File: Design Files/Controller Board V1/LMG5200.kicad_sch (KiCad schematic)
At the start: 4 parts, among them Q1 LMG5200

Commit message: yay(meeting 2/16/2025)
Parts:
- removed R1: R, symbol Device:R
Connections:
- net ADC1 renamed ADC_Pos
- net ADC3 renamed ADC_Neg
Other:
- moved on the sheet: L2
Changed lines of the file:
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@@
 	(paper "A4")
-	(junction
-		(at 139.7 81.28)
-		(diameter 0)
-		(color 0 0 0 0)
-	)
-	(junction
-		(at 139.7 71.12)
-		(diameter 0)
-		(color 0 0 0 0)
-	)
 	(junction
 		(at 139.7 66.04)
@@
 		(color 0 0 0 0)
 	)
-	(junction
-		(at 139.7 62.23)
-		(diameter 0)
-		(color 0 0 0 0)
-	)
 	(wire
 		(pts
@@
 	(wire
 		(pts
-			(xy 139.7 83.82) (xy 139.7 81.28)
+			(xy 143.51 83.82) (xy 143.51 81.28)
 		)
 		(stroke
@@
 	(wire
 		(pts
-			(xy 139.7 52.07) (xy 139.7 62.23)
-		)
-		(stroke
-			(width 0)
-			(type default)
-		)
-	)
-	(wire
-		(pts
 			(xy 143.51 125.73) (xy 143.51 134.62)
 		)
@@
 	(wire
 		(pts
-			(xy 139.7 81.28) (xy 139.7 78.74)
-		)
-		(stroke
-			(width 0)
-			(type default)
-		)
-	)
-	(wire
-		(pts
 			(xy 139.7 71.12) (xy 139.7 66.04)
 		)
@@
 	(wire
 		(pts
-			(xy 139.7 81.28) (xy 153.67 81.28)
+			(xy 143.51 81.28) (xy 153.67 81.28)
 		)
 		(stroke
@@
 		)
 	)
-	(hierarchical_label "ADC3"
+	(hierarchical_label "ADC_Neg"
 		(shape input)
 		(at 153.67 81.28 0)
@@
 		)
 	)
-	(hierarchical_label "ADC1"
-		(shape input)
-		(at 139.7 52.07 90)
-		(effects
-			(font
-				(size 1.27 1.27)
-			)
-			(justify left)
-		)
-	)
 	(hierarchical_label "bottom_out"
 		(shape input)
@@
 		)
 	)
-	(hierarchical_label "ADC2"
+	(hierarchical_label "ADC_Pos"
 		(shape input)
 		(at 153.67 71.12 0)
@@
 	(symbol
 		(lib_id "Device:L")
-		(at 139.7 87.63 0)
+		(at 143.51 87.63 0)
 		(unit 1)
 		(exclude_from_sim no)
@@
 		(fields_autoplaced yes)
 		(property "Reference" "L2"
-			(at 140.97 86.3599 0)
+			(at 144.78 86.3599 0)
 			(effects
 				(font
@@
 		)
 		(property "Value" "L"
-			(at 140.97 88.8999 0)
+			(at 144.78 88.8999 0)
 			(effects
 				(font
@@
 		)
 		(property "Footprint" ""
-			(at 139.7 87.63 0)
+			(at 143.51 87.63 0)
 			(effects
 				(font
@@
 		)
 		(property "Datasheet" "~"
-			(at 139.7 87.63 0)
+			(at 143.51 87.63 0)
 			(effects
 				(font
@@
 		)
 		(property "Description" "Inductor"
-			(at 139.7 87.63 0)
+			(at 143.51 87.63 0)
 			(effects
 				(font
@@
 					(unit 1)
 				)
-			)
-		)
-	)
-	(symbol
-		(lib_id "Device:R")
-		(at 139.7 74.93 0)
-		(unit 1)
-		(exclude_from_sim no)
-		(in_bom yes)
-		(on_board yes)
-		(dnp no)
-		(fields_autoplaced yes)
-		(property "Reference" "R1"
-			(at 142.24 73.6599 0)
-			(effects
-				(font
-					(size 1.27 1.27)
-				)
-				(justify left)
-			)
-		)
-		(property "Value" "R"
-			(at 142.24 76.1999 0)
-			(effects
-				(font
-					(size 1.27 1.27)
-				)
-				(justify left)
-			)
-		)
-		(property "Footprint" ""
-			(at 137.922 74.93 90)
-			(effects
-				(font
-					(size 1.27 1.27)
-				)
-				(hide yes)
-			)
-		)
-		(property "Datasheet" "~"
-			(at 139.7 74.93 0)
-			(effects
-				(font
-					(size 1.27 1.27)
-				)
-				(hide yes)
-			)
-		)
-		(property "Description" "Resistor"
-			(at 139.7 74.93 0)
-			(effects
-				(font
-					(size 1.27 1.27)
-				)
-				(hide yes)
-			)
-		)
-		(pin "1"
-		)
-		(pin "2"
-		)
-		(instances
-			(project "Control Board V1"
-				(path "/e0c606b8-cbb9-4aff-b96c-73876da6ca74/a6c70f8b-d576-48c3-bfc7-6e0bdb401246"
-					(reference "R1")
-					(unit 1)
-				)

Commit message: Major Schematic Progress
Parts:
- added C2, C3: 0.1u, symbol Device:C
- added R1: 39k, Resistor_SMD:R_0603_1608Metric, symbol Device:R
- added R13, R14: 2k, Resistor_SMD:R_0603_1608Metric, symbol Device:R
- added R15: 11k, Resistor_SMD:R_0603_1608Metric, symbol Device:R
- C1: value C -> 10u
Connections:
- net ADC_Neg is gone; now on an unnamed net: L2.1
- net ADC_Pos is gone; now on net cap_volt: C1.2
- net 5V: now also C2.1
- net GND: now also Q1.9, R15.2
- net PWM_bottom: now also R13.1
- net PWM_top: now also R14.1
- net cap_volt: now reaches L2.2
- net cap_volt: now also R1.1
- net high_side_FET: now reaches Q1.1
- net at Q1.2 (HB): now also C3.1
- net at Q1.3 (HS): now also C3.2
- net sig-gnd renamed A_GND
- net A_GND: now also C2.2, R13.2, R14.2
- new net cap_volt_pico_adc: R1.2, R15.1
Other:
- moved on the sheet: C1, L2, Q1

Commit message: here we go agane
Updating footprints and tackling general layout
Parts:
- C2, C3: footprint (none) -> Capacitor_SMD:C_0603_1608Metric
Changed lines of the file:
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@@
 			)
 		)
-		(property "Footprint" ""
+		(property "Footprint" "Capacitor_SMD:C_0603_1608Metric"
 			(at 108.9152 96.52 0)
 			(effects
@@
 			)
 		)
-		(property "Footprint" ""
+		(property "Footprint" "Capacitor_SMD:C_0603_1608Metric"
 			(at 113.03 84.7852 0)
 			(effects

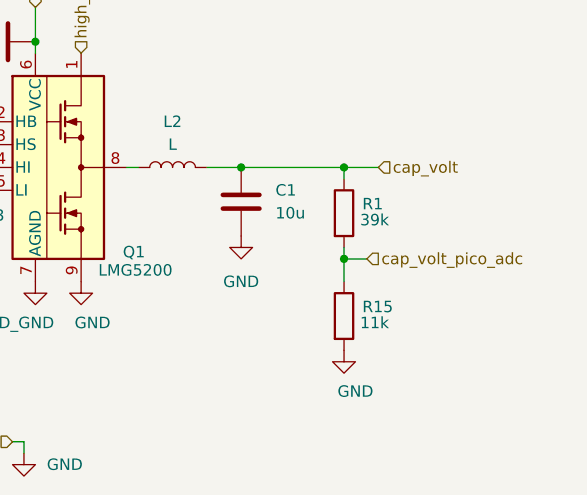
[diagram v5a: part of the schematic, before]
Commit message: current sensor done
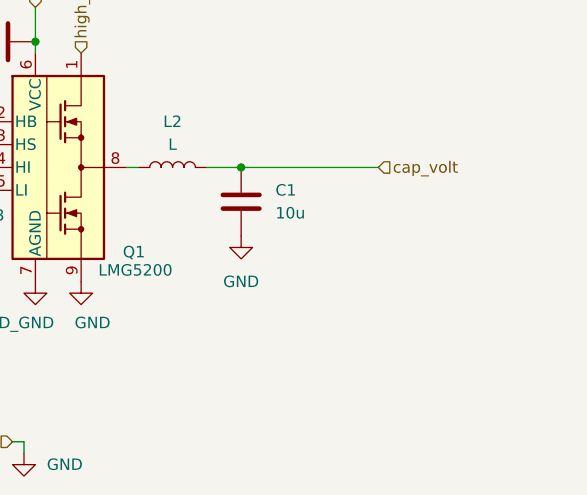
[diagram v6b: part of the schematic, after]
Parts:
- removed R1: 39k, Resistor_SMD:R_0603_1608Metric, symbol Device:R
- removed R15: 11k, Resistor_SMD:R_0603_1608Metric, symbol Device:R

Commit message: Added Cap footprint, added LED, added Resistors
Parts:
- C1: footprint (none) -> Capacitor_SMD:C_0603_1608Metric
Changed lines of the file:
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@@
 		(shape input)
 		(at 158.75 97.79 0)
+		(fields_autoplaced yes)
 		(effects
 			(font
@@
 		(shape input)
 		(at 95.25 128.27 180)
+		(fields_autoplaced yes)
 		(effects
 			(font
@@
 		(shape input)
 		(at 120.65 80.01 90)
+		(fields_autoplaced yes)
 		(effects
 			(font
@@
 		(shape input)
 		(at 118.11 128.27 180)
+		(fields_autoplaced yes)
 		(effects
 			(font
@@
 		(shape input)
 		(at 110.49 100.33 180)
+		(fields_autoplaced yes)
 		(effects
 			(font
@@
 		(shape input)
 		(at 88.9 97.79 180)
+		(fields_autoplaced yes)
 		(effects
 			(font
@@
 		(shape input)
 		(at 125.73 85.09 90)
+		(fields_autoplaced yes)
 		(effects
 			(font
@@
 			)
 		)
-		(property "Footprint" ""
+		(property "Footprint" "Capacitor_SMD:C_0603_1608Metric"
 			(at 142.5448 97.79 0)
 			(effects

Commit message: half finished with brooks changes
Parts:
- added C12: 10u, Capacitor_SMD:C_0603_1608Metric, symbol Device:C
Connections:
- net GND: now also C12.1; no longer C1.1, Q1.9
- net A_GND renamed D_GND
- net D_GND: no longer Q1.7 (AGND)
- new net P_GND: C1.1, Q1.7 (AGND), Q1.9
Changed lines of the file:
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@@
-	(wire
-		(pts
-			(xy 97.79 129.54) (xy 97.79 128.27)
-		)
-		(stroke
-			(width 0)
-			(type default)
-		)
-	)
 	(wire
 		(pts
@@
 	(wire
 		(pts
-			(xy 119.38 128.27) (xy 118.11 128.27)
-		)
-		(stroke
-			(width 0)
-			(type default)
-		)
-	)
-	(wire
-		(pts
 			(xy 130.81 97.79) (xy 132.08 97.79)
 		)
@@
 	(wire
 		(pts
-			(xy 97.79 128.27) (xy 95.25 128.27)
-		)
-		(stroke
-			(width 0)
-			(type default)
-		)
-	)
-	(wire
-		(pts
-			(xy 119.38 128.27) (xy 119.38 129.54)
+			(xy 125.73 86.36) (xy 132.08 86.36)
 		)
 		(stroke
@@
 		)
 	)
-	(hierarchical_label "D_GND"
-		(shape input)
-		(at 95.25 128.27 180)
-		(fields_autoplaced yes)
-		(effects
-			(font
-				(size 1.27 1.27)
-			)
-			(justify right)
-		)
-	)
 	(hierarchical_label "5V"
 		(shape input)
@@
 		)
 	)
-	(hierarchical_label "P_GND"
-		(shape input)
-		(at 118.11 128.27 180)
-		(fields_autoplaced yes)
-		(effects
-			(font
-				(size 1.27 1.27)
-			)
-			(justify right)
-		)
-	)
 	(hierarchical_label "PWM_bottom"
 		(shape input)
@@
 			)
 		)
-		(property "Value" "GND"
+		(property "Value" "P_GND"
 			(at 127 115.062 0)
 			(effects
@@
 	(symbol
 		(lib_id "Device:C")
+		(at 135.89 86.36 270)
+		(unit 1)
+		(exclude_from_sim no)
+		(in_bom yes)
+		(on_board yes)
+		(dnp no)
+		(fields_autoplaced yes)
+		(property "Reference" "C12"
+			(at 134.6199 82.55 0)
+			(effects
+				(font
+					(size 1.27 1.27)
+				)
+				(justify right)
+			)
+		)
+		(property "Value" "10u"
+			(at 137.1599 82.55 0)
+			(effects
+				(font
+					(size 1.27 1.27)
+				)
+				(justify right)
+			)
+		)
+		(property "Footprint" "Capacitor_SMD:C_0603_1608Metric"
+			(at 132.08 87.3252 0)
+			(effects
+				(font
+					(size 1.27 1.27)
+				)
+				(hide yes)
+			)
+		)
+		(property "Datasheet" "~"
+			(at 135.89 86.36 0)
+			(effects
+				(font
+					(size 1.27 1.27)
+				)
+				(hide yes)
+			)
+		)
+		(property "Description" "Unpolarized capacitor"
+			(at 135.89 86.36 0)
+			(effects
+				(font
+					(size 1.27 1.27)
+				)
+				(hide yes)
+			)
+		)
+		(pin "1"
+		)
+		(pin "2"
+		)
+		(instances
+			(project "Control Board V1"
+				(path "/e0c606b8-cbb9-4aff-b96c-73876da6ca74/a6c70f8b-d576-48c3-bfc7-6e0bdb401246"
+					(reference "C12")
+					(unit 1)
+				)
+			)
+		)
+	)
+	(symbol
+		(lib_id "Device:C")
 		(at 107.95 92.71 0)
 		(unit 1)
@@
 				(path "/e0c606b8-cbb9-4aff-b96c-73876da6ca74/a6c70f8b-d576-48c3-bfc7-6e0bdb401246"
 					(reference "C3")
-					(unit 1)
-				)
-			)
-		)
-	)
-	(symbol
-		(lib_id "power:GND")
-		(at 97.79 129.54 0)
-		(unit 1)
-		(exclude_from_sim no)
-		(in_bom yes)
-		(on_board yes)
-		(dnp no)
-		(property "Reference" "#PWR014"
-			(at 97.79 135.89 0)
-			(effects
-				(font
-					(size 1.27 1.27)
-				)
-				(hide yes)
-			)
-		)
-		(property "Value" "A_GND"
-			(at 103.124 130.81 0)
-			(effects
-				(font
-					(size 1.27 1.27)
-				)
-			)
-		)
-		(property "Footprint" ""
-			(at 97.79 129.54 0)
-			(effects
-				(font
-					(size 1.27 1.27)
-				)
-				(hide yes)
-			)
-		)
-		(property "Datasheet" ""
-			(at 97.79 129.54 0)
-			(effects
-				(font
-					(size 1.27 1.27)
-				)
-				(hide yes)
-			)
-		)
-		(property "Description" "Power symbol creates a global label with name \"GND\" , ground"
-			(at 97.79 129.54 0)
-			(effects
-				(font
-					(size 1.27 1.27)
-				)
-				(hide yes)
-			)
-		)
-		(pin "1"
-		)
-		(instances
-			(project "Control Board V1"
-				(path "/e0c606b8-cbb9-4aff-b96c-73876da6ca74/a6c70f8b-d576-48c3-bfc7-6e0bdb401246"
-					(reference "#PWR014")
-					(unit 1)
-				)
-			)
-		)
-	)
-	(symbol
-		(lib_id "power:GND")
-		(at 119.38 129.54 0)
-		(unit 1)
-		(exclude_from_sim no)
-		(in_bom yes)
-		(on_board yes)
-		(dnp no)
-		(fields_autoplaced yes)
-		(property "Reference" "#PWR01"
-			(at 119.38 135.89 0)
-			(effects
-				(font
-					(size 1.27 1.27)
-				)
-				(hide yes)
-			)
-		)
-		(property "Value" "GND"
-			(at 121.92 130.8099 0)
-			(effects
-				(font
-					(size 1.27 1.27)
-				)
-				(justify left)
-			)
-		)
-		(property "Footprint" ""
-			(at 119.38 129.54 0)
-			(effects
-				(font
-					(size 1.27 1.27)
-				)
-				(hide yes)
-			)
-		)
-		(property "Datasheet" ""
-			(at 119.38 129.54 0)
-			(effects
-				(font
-					(size 1.27 1.27)
-				)
-				(hide yes)
-			)
-		)
-		(property "Description" "Power symbol creates a global label with name \"GND\" , ground"
-			(at 119.38 129.54 0)
-			(effects
-				(font
-					(size 1.27 1.27)
-				)
-				(hide yes)
-			)
-		)
-		(pin "1"
-		)
-		(instances
-			(project "Control Board V1"
-				(path "/e0c606b8-cbb9-4aff-b96c-73876da6ca74/a6c70f8b-d576-48c3-bfc7-6e0bdb401246"
-					(reference "#PWR01")
 					(unit 1)
 				)
@@
 			)
 		)
-		(property "Value" "D_GND"
+		(property "Value" "P_GND"
 			(at 119.634 115.062 0)
 			(effects
@@
 				(path "/e0c606b8-cbb9-4aff-b96c-73876da6ca74/a6c70f8b-d576-48c3-bfc7-6e0bdb401246"
 					(reference "#PWR015")
+					(unit 1)
+				)
+			)
+		)
+	)
+	(symbol
+		(lib_id "power:GND")
+		(at 139.7 86.36 90)
+		(unit 1)
+		(exclude_from_sim no)
+		(in_bom yes)
+		(on_board yes)
+		(dnp no)
+		(property "Reference" "#PWR037"
+			(at 146.05 86.36 0)
+			(effects
+				(font
+					(size 1.27 1.27)
+				)
+				(hide yes)
+			)
+		)
+		(property "Value" "GND"
+			(at 144.272 85.09 0)
+			(effects
+				(font
+					(size 1.27 1.27)
+				)
+			)
+		)
+		(property "Footprint" ""
+			(at 139.7 86.36 0)
+			(effects
+				(font
+					(size 1.27 1.27)
+				)
+				(hide yes)
+			)
+		)
+		(property "Datasheet" ""
+			(at 139.7 86.36 0)
+			(effects
+				(font
+					(size 1.27 1.27)
+				)
+				(hide yes)
+			)
+		)
+		(property "Description" "Power symbol creates a global label with name \"GND\" , ground"
+			(at 139.7 86.36 0)
+			(effects
+				(font
+					(size 1.27 1.27)
+				)
+				(hide yes)
+			)
+		)
+		(pin "1"
+		)
+		(instances
+			(project "Control Board V1"
+				(path "/e0c606b8-cbb9-4aff-b96c-73876da6ca74/a6c70f8b-d576-48c3-bfc7-6e0bdb401246"
+					(reference "#PWR037")
 					(unit 1)
 				)
@@
 			)
 		)
-		(property "Value" "GND"
+		(property "Value" "P_GND"
 			(at 143.51 110.49 0)
 			(effects
